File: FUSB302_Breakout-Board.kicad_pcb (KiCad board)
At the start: 2 copper layers, 19 x 19 mm, 4 parts, among them J1 Conn_01x07_Male, J2 Conn_01x07_Male, U1 FUSB302BMPX

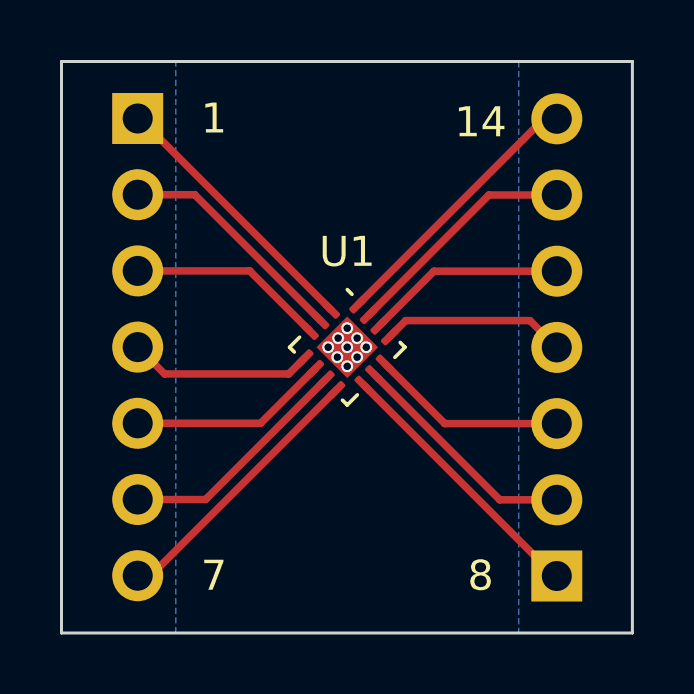
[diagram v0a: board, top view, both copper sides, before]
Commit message: Mod: Updated the project name and revision to be on the copper layer now
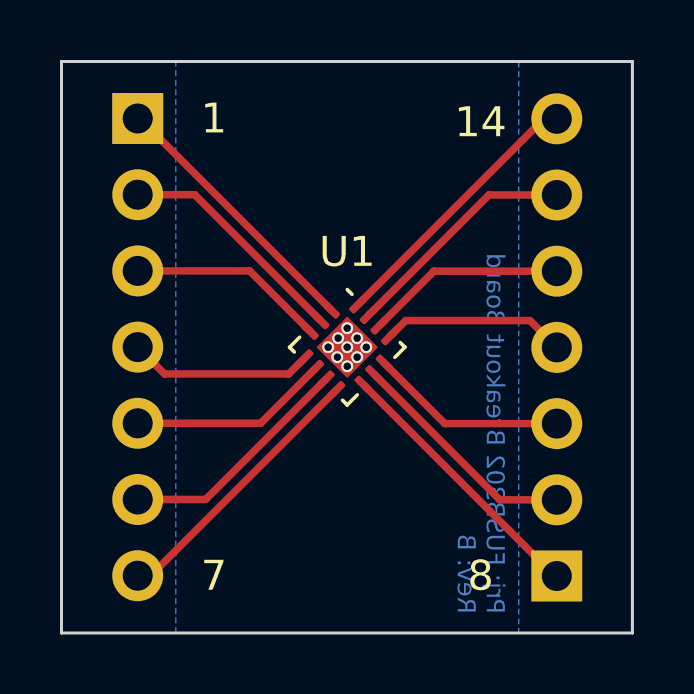
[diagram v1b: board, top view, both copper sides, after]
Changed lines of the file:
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@@
   (title_block
     (title "FUSB302 Breakout Board")
-    (date "2023-03-06")
-    (rev "A")
+    (date "2023-03-07")
+    (rev "B")
     (company "ElektroNik Zoller")
-    (comment 1 "Author: Nikolai Zoller")
-    (comment 4 "License: CERN-OHL-P")
+    (comment 1 "Nikolai Zoller")
+    (comment 4 "CERN-OHL-P")
   )
   (layers
@@
     (property "Sheetname" "")
     (attr through_hole)
-    (fp_text reference "J2" (at -3.175 -0.005) (layer "B.SilkS")
+    (fp_text reference "J2" (at -3.175 -15.245) (layer "B.SilkS")
       (effects (font (size 1 1) (thickness 0.15)) (justify mirror))
     )
@@
   )
   (gr_rect (start 140.335 105.41) (end 159.365 124.46) (layer "Edge.Cuts") (width 0.1) (fill none))
+  (gr_text "Prj: ${TITLE}\nRev: ${REVISION}" (at 154.305 123.825 270) (layer "B.Cu")
+    (effects (font (size 0.6 0.6) (thickness 0.15)) (justify left mirror))
+  )
   (gr_text "7" (at 145.415 122.555) (layer "F.SilkS")
     (effects (font (size 1 1) (thickness 0.15)))
@@
     (effects (font (size 1 1) (thickness 0.15)))
   )
-  (gr_text "Prj: ${TITLE}\nRev: ${REVISION}" (at 149.86 120.65) (layer "B.Mask")
-    (effects (font (size 0.4 0.4) (thickness 0.1)) (justify mirror))
-  )
   (segment (start 156.845 114.94) (end 155.951 114.046) (width 0.25) (layer "F.Cu") (net 1))

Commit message: Mod: The project name string
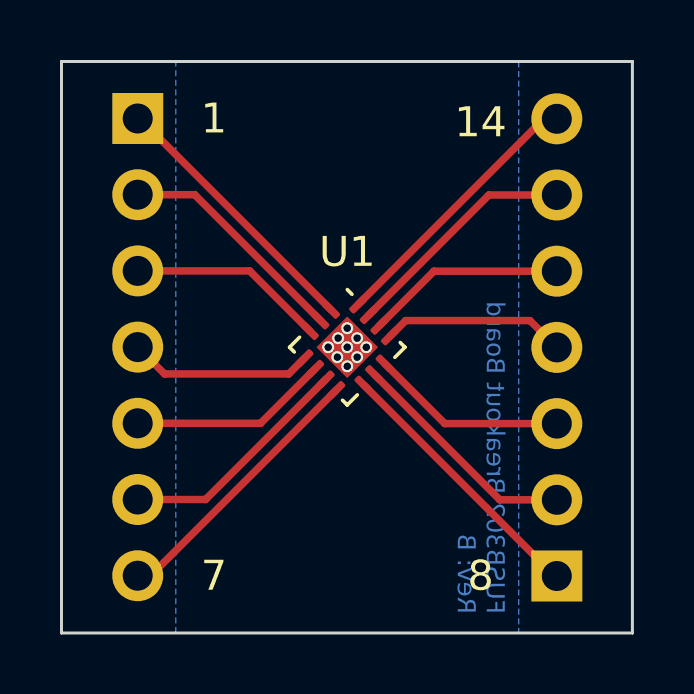
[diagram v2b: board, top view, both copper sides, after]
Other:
- board text added: "${TITLE} Rev: ${REVISION}"
- board text removed: "Prj: ${TITLE} Rev: ${REVISION}"
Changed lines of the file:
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@@
   )
   (gr_rect (start 140.335 105.41) (end 159.365 124.46) (layer "Edge.Cuts") (width 0.1) (fill none))
-  (gr_text "Prj: ${TITLE}\nRev: ${REVISION}" (at 154.305 123.825 270) (layer "B.Cu")
+  (gr_text "${TITLE}\nRev: ${REVISION}" (at 154.305 123.825 270) (layer "B.Cu")
     (effects (font (size 0.6 0.6) (thickness 0.15)) (justify left mirror))
   )
